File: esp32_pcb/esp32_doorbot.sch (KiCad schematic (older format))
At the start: 15 parts, among them J2 Conn_01x02_Female, J3 Conn_01x08, J4 Conn_01x06, Q1 2N7002E, U1 L7805, U2 74LVC2T45DC

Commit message: Use header that attaches to wesp32 board directly
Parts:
- J3: value Conn_01x08 -> ESP32; footprint Pin_Headers:Pin_Header_Straight_1x08 -> Pin_Headers:Pin_Header_Straight_2x10; symbol Connector_Generic:Conn_01x08 -> Connector_Generic:Conn_02x10_Odd_Even
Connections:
- no-connect marks 0 -> 12
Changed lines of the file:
@@
 Wire Wire Line
 	1650 3800 1500 3800
-Text GLabel 5200 1300 0    50   Input ~ 0
+Text GLabel 4050 1150 0    50   Input ~ 0
 12V
 $Comp
 L power:GND #PWR0104
 U 1 1 605FBF90
-P 5400 2050
-F 0 "#PWR0104" H 5400 1800 50  0001 C CNN
-F 1 "GND" H 5405 1877 50  0000 C CNN
-F 2 "" H 5400 2050 50  0001 C CNN
-F 3 "" H 5400 2050 50  0001 C CNN
-	1    5400 2050
-	1    0    0    -1
-$EndComp
-Text GLabel 5200 1500 0    50   Input ~ 0
+P 5550 1150
+F 0 "#PWR0104" H 5550 900 50  0001 C CNN
+F 1 "GND" H 5555 977 50  0000 C CNN
+F 2 "" H 5550 1150 50  0001 C CNN
+F 3 "" H 5550 1150 50  0001 C CNN
+	1    5550 1150
+	1    0    0    -1
+$EndComp
+Text GLabel 4050 1350 0    50   Input ~ 0
 DOOR
-Text GLabel 5200 1600 0    50   Input ~ 0
+Text GLabel 4050 1250 0    50   Input ~ 0
 WIEGAND_OUT1
-Text GLabel 5200 1700 0    50   Input ~ 0
+Text GLabel 4850 1350 2    50   Input ~ 0
 WIEGAND_OUT2
 $Comp
@@
 Text GLabel 5150 4950 1    50   Input ~ 0
 5V
-Text GLabel 5200 1400 0    50   Input ~ 0
+Text GLabel 4100 2050 0    50   Input ~ 0
 3.3V
-Wire Wire Line
-	5200 1300 5400 1300
-Wire Wire Line
-	5400 1400 5200 1400
-Wire Wire Line
-	5200 1500 5400 1500
-Wire Wire Line
-	5400 1600 5200 1600
-Wire Wire Line
-	5200 1700 5400 1700
 Text GLabel 5350 4950 1    50   Input ~ 0
 3.3V
@@
 Wire Wire Line
 	5250 6400 5250 6150
-Text GLabel 5200 1900 0    50   Input ~ 0
+Text GLabel 4050 1550 0    50   Input ~ 0
 READER_LED
-Text GLabel 5200 1800 0    50   Input ~ 0
+Text GLabel 4050 1450 0    50   Input ~ 0
 READER_BUZZ
 $Comp
-L Connector_Generic:Conn_01x08 J3
+L Connector_Generic:Conn_02x10_Odd_Even J3
 U 1 1 6063C556
-P 5600 1600
-F 0 "J3" H 5680 1592 50  0000 L CNN
-F 1 "Conn_01x08" H 5680 1501 50  0000 L CNN
-F 2 "Pin_Headers:Pin_Header_Straight_1x08" H 5600 1600 50  0001 C CNN
-F 3 "~" H 5600 1600 50  0001 C CNN
-	1    5600 1600
-	1    0    0    -1
-$EndComp
-Wire Wire Line
-	5200 1800 5400 1800
-Wire Wire Line
-	5400 1900 5200 1900
-Wire Wire Line
-	5400 2050 5400 2000
+P 4500 1650
+F 0 "J3" H 4500 2300 50  0000 L CNN
+F 1 "ESP32" H 4450 2200 50  0000 L CNN
+F 2 "Pin_Headers:Pin_Header_Straight_2x10" H 4500 1650 50  0001 C CNN
+F 3 "~" H 4500 1650 50  0001 C CNN
+	1    4500 1650
+	-1   0    0    1
+$EndComp
 $Comp
 L Connector_Generic:Conn_01x06 J4
@@
 Wire Wire Line
 	6400 1450 7350 1450
+Wire Wire Line
+	4200 1150 4050 1150
+Wire Wire Line
+	4050 1250 4200 1250
+Wire Wire Line
+	4200 1350 4050 1350
+Wire Wire Line
+	4050 1450 4200 1450
+Wire Wire Line
+	4200 1550 4050 1550
+Wire Wire Line
+	4100 2050 4200 2050
+Wire Wire Line
+	4700 1350 4850 1350
+Wire Wire Line
+	4700 1150 5550 1150
+NoConn ~ 4700 1250
+NoConn ~ 4700 1450
+NoConn ~ 4700 1550
+NoConn ~ 4700 1650
+NoConn ~ 4700 1750
+NoConn ~ 4700 1850
+NoConn ~ 4700 1950
+NoConn ~ 4700 2050
+NoConn ~ 4200 1950
+NoConn ~ 4200 1850
+NoConn ~ 4200 1750
+NoConn ~ 4200 1650
 $EndSCHEMATC

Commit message: Add part number for 2x10 pin header
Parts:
- J3: Digikey # (none) -> S6106-ND‎
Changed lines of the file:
@@
 F 2 "Pin_Headers:Pin_Header_Straight_2x10" H 4500 1650 50  0001 C CNN
 F 3 "~" H 4500 1650 50  0001 C CNN
+F 4 "S6106-ND‎" H 4500 1650 50  0001 C CNN "Digikey #"
 	1    4500 1650
 	-1   0    0    1

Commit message: Change schematic for regular ESP32, not a PoE version
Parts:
- removed J3: ESP32, Pin_Headers:Pin_Header_Straight_2x10, symbol Connector_Generic:Conn_02x10_Odd_Even
- removed J4: Conn_01x06, Pin_Headers:Pin_Header_Straight_1x06, symbol Connector_Generic:Conn_01x06
- added J1: Conn_01x07_Male, Pin_Headers:Pin_Header_Straight_1x07, symbol Connector:Conn_01x07_Male
- added J3: Barrel_Jack, Terminal_Blocks:TerminalBlock_Pheonix_MKDS1.5-2pol, symbol Connector:Barrel_Jack
- added J4: WROOM32_1, Pin_Headers:Pin_Header_Straight_1x15, symbol Connector:Conn_01x15_Female
- added J5: WROOM32_2, Pin_Headers:Pin_Header_Straight_1x15, symbol Connector:Conn_01x15_Female
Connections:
- net labels added: 24_32_SWITCH
- wire segments 51 -> 55
- no-connect marks 12 -> 21
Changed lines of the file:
@@
 Wire Wire Line
 	1650 3800 1500 3800
-Text GLabel 4050 1150 0    50   Input ~ 0
-12V
-$Comp
-L power:GND #PWR0104
-U 1 1 605FBF90
-P 5550 1150
-F 0 "#PWR0104" H 5550 900 50  0001 C CNN
-F 1 "GND" H 5555 977 50  0000 C CNN
-F 2 "" H 5550 1150 50  0001 C CNN
-F 3 "" H 5550 1150 50  0001 C CNN
-	1    5550 1150
-	1    0    0    -1
-$EndComp
-Text GLabel 4050 1350 0    50   Input ~ 0
+Text GLabel 9050 3300 2    50   Input ~ 0
 DOOR
-Text GLabel 4050 1250 0    50   Input ~ 0
+Text GLabel 7800 3300 0    50   Input ~ 0
 WIEGAND_OUT1
-Text GLabel 4850 1350 2    50   Input ~ 0
-WIEGAND_OUT2
 $Comp
 L Regulator_Linear:L7805 U1
@@
 Text GLabel 5150 4950 1    50   Input ~ 0
 5V
-Text GLabel 4100 2050 0    50   Input ~ 0
-3.3V
 Text GLabel 5350 4950 1    50   Input ~ 0
 3.3V
@@
 Wire Wire Line
 	5250 6400 5250 6150
-Text GLabel 4050 1550 0    50   Input ~ 0
+Text GLabel 9050 3100 2    50   Input ~ 0
 READER_LED
-Text GLabel 4050 1450 0    50   Input ~ 0
+Text GLabel 9050 3200 2    50   Input ~ 0
 READER_BUZZ
-$Comp
-L Connector_Generic:Conn_02x10_Odd_Even J3
-U 1 1 6063C556
-P 4500 1650
-F 0 "J3" H 4500 2300 50  0000 L CNN
-F 1 "ESP32" H 4450 2200 50  0000 L CNN
-F 2 "Pin_Headers:Pin_Header_Straight_2x10" H 4500 1650 50  0001 C CNN
-F 3 "~" H 4500 1650 50  0001 C CNN
-F 4 "S6106-ND‎" H 4500 1650 50  0001 C CNN "Digikey #"
-	1    4500 1650
-	-1   0    0    1
-$EndComp
-$Comp
-L Connector_Generic:Conn_01x06 J4
-U 1 1 60640874
-P 7550 1550
-F 0 "J4" H 7630 1542 50  0000 L CNN
-F 1 "Conn_01x06" H 7630 1451 50  0000 L CNN
-F 2 "Pin_Headers:Pin_Header_Straight_1x06" H 7550 1550 50  0001 C CNN
-F 3 "~" H 7550 1550 50  0001 C CNN
-	1    7550 1550
-	1    0    0    -1
-$EndComp
-Text GLabel 7150 1350 0    50   Input ~ 0
+Text GLabel 3550 1250 0    50   Input ~ 0
 12V
-Text GLabel 7150 1550 0    50   Input ~ 0
+Text GLabel 3550 1450 0    50   Input ~ 0
 WIEGAND_IN1
-Text GLabel 7150 1650 0    50   Input ~ 0
+Text GLabel 3550 1550 0    50   Input ~ 0
 WIEGAND_IN2
-Text GLabel 7150 1850 0    50   Input ~ 0
+Text GLabel 3550 1750 0    50   Input ~ 0
 READER_LED
-Text GLabel 7150 1750 0    50   Input ~ 0
+Text GLabel 3550 1650 0    50   Input ~ 0
 READER_BUZZ
 $Comp
 L power:GND #PWR0109
 U 1 1 60644B08
-P 6400 1450
-F 0 "#PWR0109" H 6400 1200 50  0001 C CNN
-F 1 "GND" H 6405 1277 50  0000 C CNN
-F 2 "" H 6400 1450 50  0001 C CNN
-F 3 "" H 6400 1450 50  0001 C CNN
-	1    6400 1450
-	1    0    0    -1
-$EndComp
-Wire Wire Line
-	7150 1350 7350 1350
-Wire Wire Line
-	7150 1550 7350 1550
-Wire Wire Line
-	7350 1650 7150 1650
-Wire Wire Line
-	7150 1750 7350 1750
+P 2800 1350
+F 0 "#PWR0109" H 2800 1100 50  0001 C CNN
+F 1 "GND" H 2805 1177 50  0000 C CNN
+F 2 "" H 2800 1350 50  0001 C CNN
+F 3 "" H 2800 1350 50  0001 C CNN
+	1    2800 1350
+	1    0    0    -1
+$EndComp
+Wire Wire Line
+	3550 1250 3750 1250
+Wire Wire Line
+	3550 1450 3750 1450
+Wire Wire Line
+	3750 1550 3550 1550
+Wire Wire Line
+	3550 1650 3750 1650
 Text GLabel 1200 950  1    50   Input ~ 0
 12V
@@
 	1200 1100 1200 950
 Wire Wire Line
-	7350 1850 7150 1850
-Wire Wire Line
-	6400 1450 7350 1450
-Wire Wire Line
-	4200 1150 4050 1150
-Wire Wire Line
-	4050 1250 4200 1250
-Wire Wire Line
-	4200 1350 4050 1350
-Wire Wire Line
-	4050 1450 4200 1450
-Wire Wire Line
-	4200 1550 4050 1550
-Wire Wire Line
-	4100 2050 4200 2050
-Wire Wire Line
-	4700 1350 4850 1350
-Wire Wire Line
-	4700 1150 5550 1150
-NoConn ~ 4700 1250
-NoConn ~ 4700 1450
-NoConn ~ 4700 1550
-NoConn ~ 4700 1650
-NoConn ~ 4700 1750
-NoConn ~ 4700 1850
-NoConn ~ 4700 1950
-NoConn ~ 4700 2050
-NoConn ~ 4200 1950
-NoConn ~ 4200 1850
-NoConn ~ 4200 1750
-NoConn ~ 4200 1650
+	2800 1350 3750 1350
+$Comp
+L Connector:Conn_01x07_Male J1
+U 1 1 608355C5
+P 3950 1550
+F 0 "J1" V 3785 1528 50  0000 C CNN
+F 1 "Conn_01x07_Male" V 3876 1528 50  0000 C CNN
+F 2 "Pin_Headers:Pin_Header_Straight_1x07" H 3950 1550 50  0001 C CNN
+F 3 "~" H 3950 1550 50  0001 C CNN
+	1    3950 1550
+	-1   0    0    1
+$EndComp
+Wire Wire Line
+	3550 1750 3750 1750
+Text GLabel 3550 1850 0    50   Input ~ 0
+24_32_SWITCH
+Wire Wire Line
+	3550 1850 3750 1850
+$Comp
+L Connector:Barrel_Jack J3
+U 1 1 60844277
+P 5750 1450
+F 0 "J3" H 5807 1775 50  0000 C CNN
+F 1 "Barrel_Jack" H 5807 1684 50  0000 C CNN
+F 2 "Terminal_Blocks:TerminalBlock_Pheonix_MKDS1.5-2pol" H 5800 1410 50  0001 C CNN
+F 3 "~" H 5800 1410 50  0001 C CNN
+	1    5750 1450
+	1    0    0    -1
+$EndComp
+$Comp
+L power:GND #PWR0102
+U 1 1 60845424
+P 6050 1700
+F 0 "#PWR0102" H 6050 1450 50  0001 C CNN
+F 1 "GND" H 6055 1527 50  0000 C CNN
+F 2 "" H 6050 1700 50  0001 C CNN
+F 3 "" H 6050 1700 50  0001 C CNN
+	1    6050 1700
+	1    0    0    -1
+$EndComp
+Text GLabel 6200 1350 2    50   Input ~ 0
+12V
+Wire Wire Line
+	6050 1350 6200 1350
+Wire Wire Line
+	6050 1550 6050 1700
+$Comp
+L power:GND #PWR0104
+U 1 1 6084B334
+P 7250 3400
+F 0 "#PWR0104" H 7250 3150 50  0001 C CNN
+F 1 "GND" H 7255 3227 50  0000 C CNN
+F 2 "" H 7250 3400 50  0001 C CNN
+F 3 "" H 7250 3400 50  0001 C CNN
+	1    7250 3400
+	1    0    0    -1
+$EndComp
+Text GLabel 7550 3500 0    50   Input ~ 0
+5V
+Text GLabel 7800 3200 0    50   Input ~ 0
+WIEGAND_OUT2
+$Comp
+L Connector:Conn_01x15_Female J4
+U 1 1 608610DB
+P 8150 2800
+F 0 "J4" H 8178 2826 50  0000 L CNN
+F 1 "WROOM32_1" H 8178 2735 50  0000 L CNN
+F 2 "Pin_Headers:Pin_Header_Straight_1x15" H 8150 2800 50  0001 C CNN
+F 3 "~" H 8150 2800 50  0001 C CNN
+	1    8150 2800
+	1    0    0    -1
+$EndComp
+$Comp
+L Connector:Conn_01x15_Female J5
+U 1 1 60861B21
+P 8700 2800
+F 0 "J5" H 8592 1875 50  0000 C CNN
+F 1 "WROOM32_2" H 8592 1966 50  0000 C CNN
+F 2 "Pin_Headers:Pin_Header_Straight_1x15" H 8700 2800 50  0001 C CNN
+F 3 "~" H 8700 2800 50  0001 C CNN
+	1    8700 2800
+	-1   0    0    1
+$EndComp
+Wire Wire Line
+	7550 3500 7950 3500
+Wire Wire Line
+	7950 3400 7250 3400
+Wire Wire Line
+	7800 3300 7950 3300
+Wire Wire Line
+	7950 3200 7800 3200
+Wire Wire Line
+	8900 3100 9050 3100
+Wire Wire Line
+	9050 3200 8900 3200
+Wire Wire Line
+	8900 3300 9050 3300
+Text GLabel 9050 3500 2    50   Input ~ 0
+3.3V
+Wire Wire Line
+	8900 3500 9050 3500
+Text GLabel 7800 3100 0    50   Input ~ 0
+24_32_SWITCH
+Wire Wire Line
+	7800 3100 7950 3100
+NoConn ~ 7950 3000
+NoConn ~ 7950 2900
+NoConn ~ 7950 2800
+NoConn ~ 7950 2700
+NoConn ~ 7950 2600
+NoConn ~ 7950 2500
+NoConn ~ 7950 2400
+NoConn ~ 7950 2300
+NoConn ~ 7950 2200
+NoConn ~ 7950 2100
+NoConn ~ 8900 2100
+NoConn ~ 8900 2200
+NoConn ~ 8900 2300
+NoConn ~ 8900 2400
+NoConn ~ 8900 2500
+NoConn ~ 8900 2600
+NoConn ~ 8900 2700
+NoConn ~ 8900 2800
+NoConn ~ 8900 2900
+NoConn ~ 8900 3000
+NoConn ~ 8900 3400
 $EndSCHEMATC

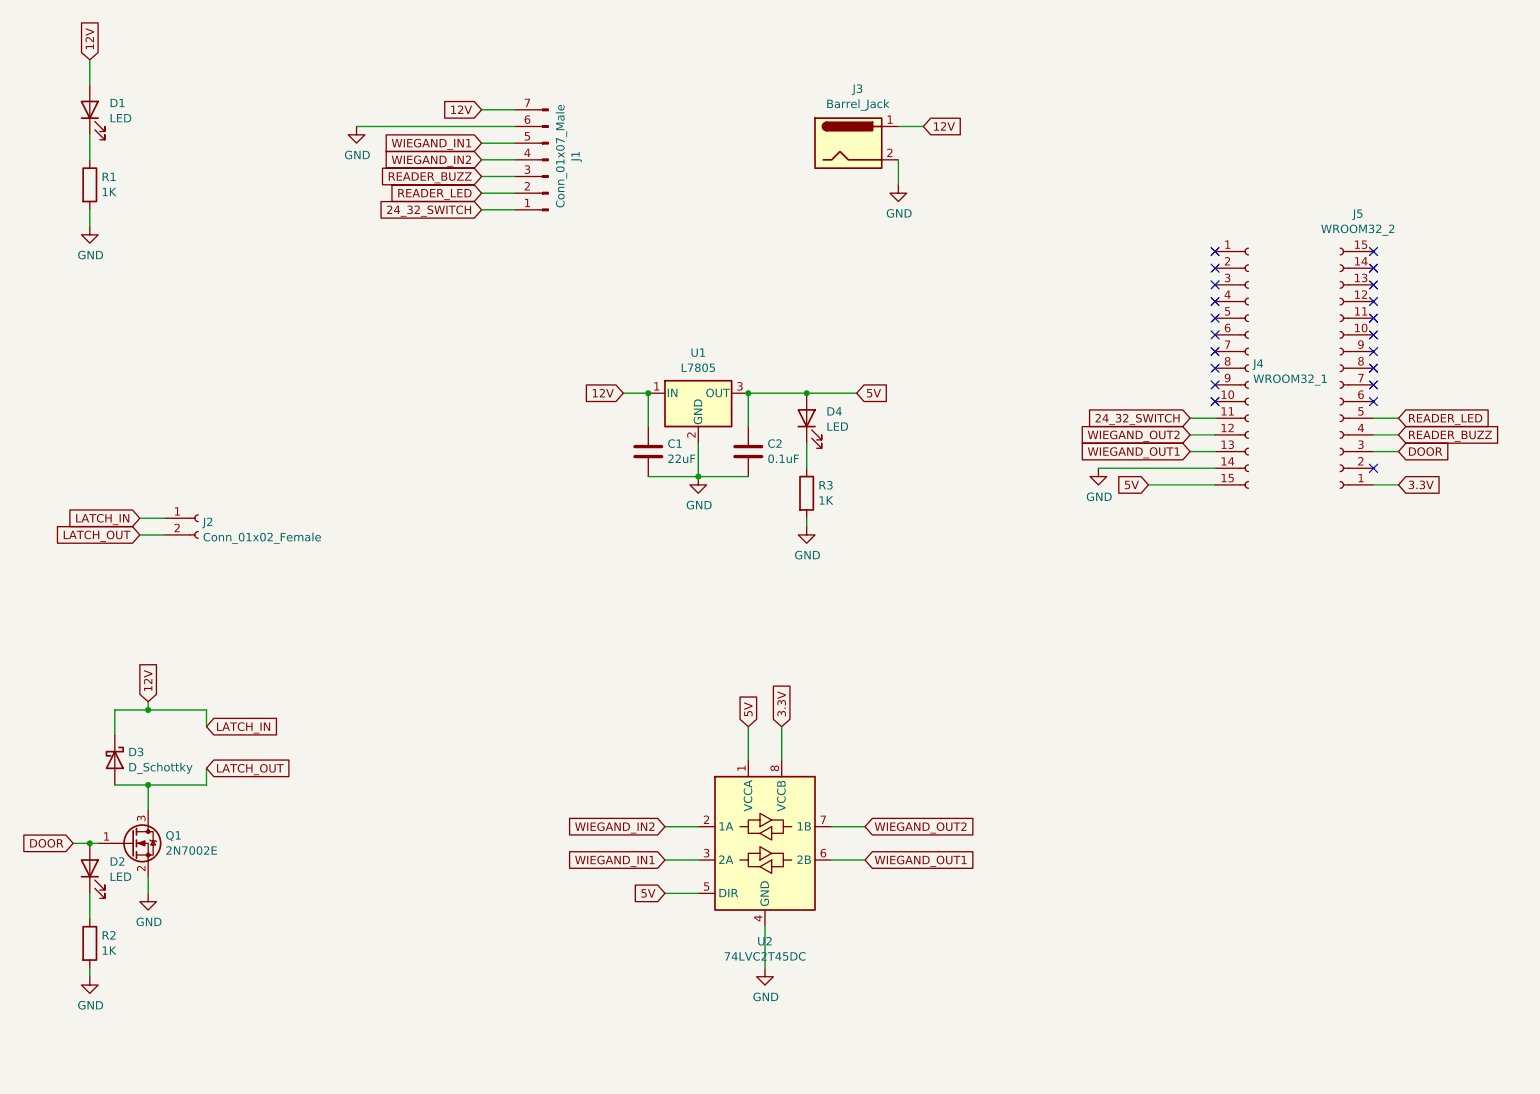
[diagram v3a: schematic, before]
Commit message: New layout for regular esp32
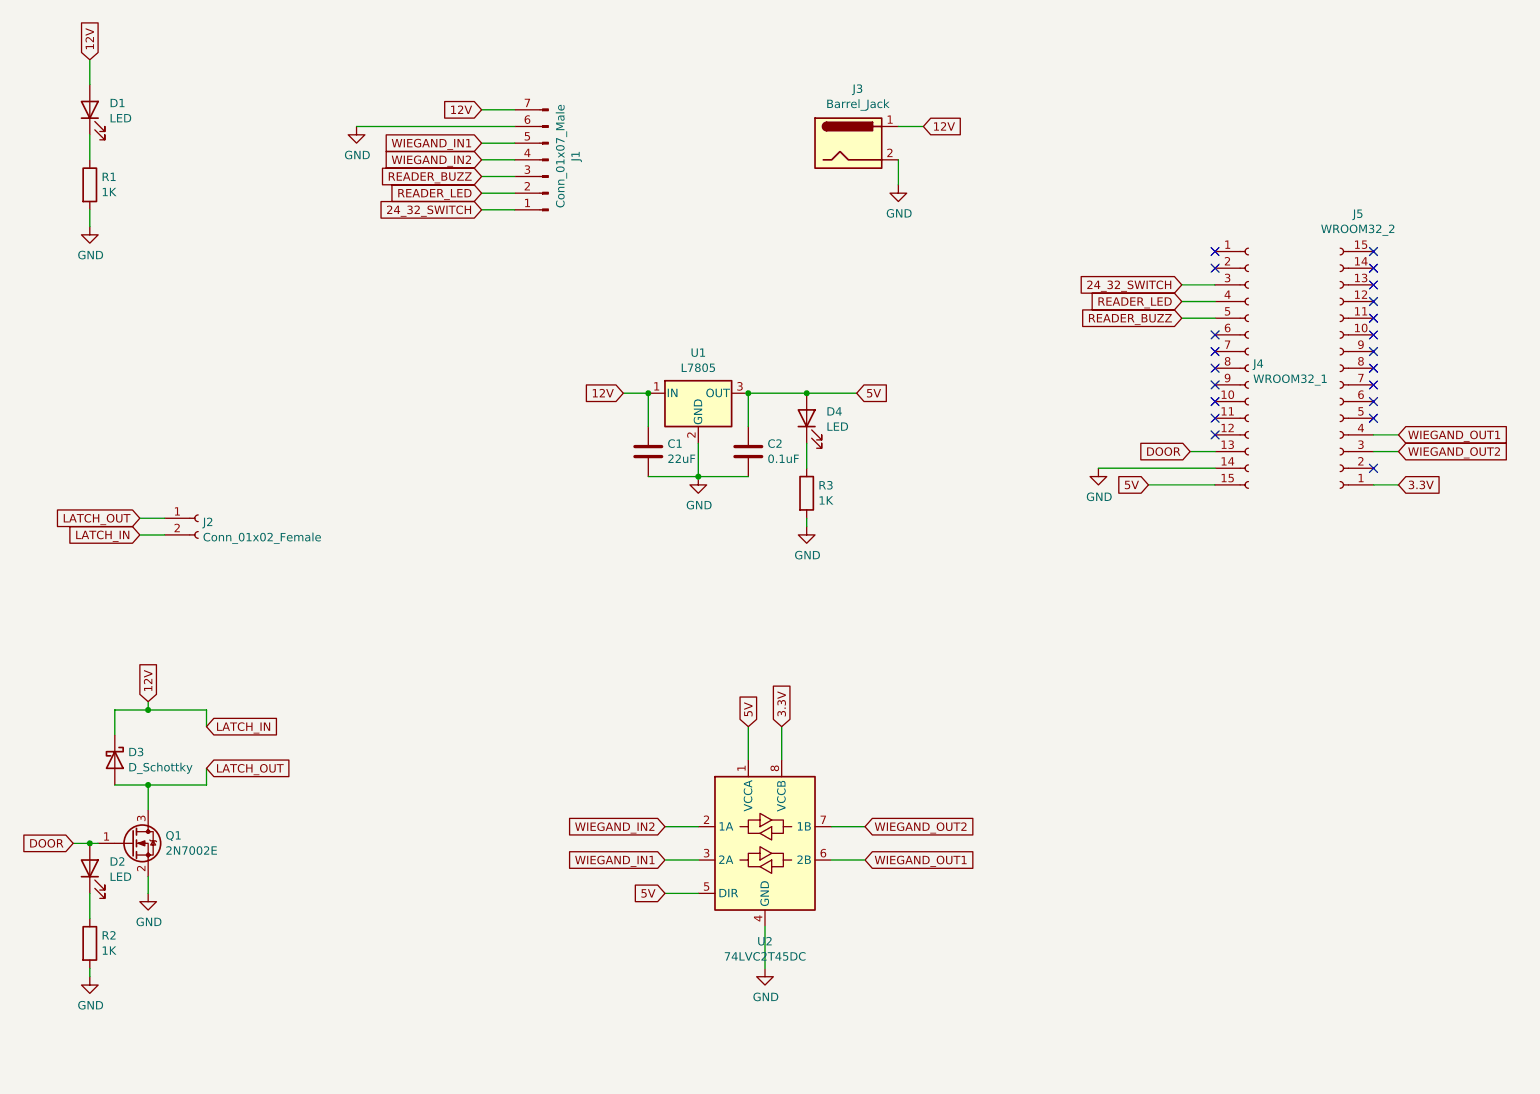
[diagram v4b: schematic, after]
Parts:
- D1, D2, D4: footprint LEDs:LED-0603 -> LEDs:LED_0603
- U2: footprint Tinkerforge-kicad:VSSOP8 -> tinkerforge-kicad:VSSOP8
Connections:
- net 12V: now also J2.2 (Pin_2); no longer J2.1 (Pin_1)
- net 24_32_SWITCH: now also J4.3 (Pin_3); no longer J4.11 (Pin_11)
- net DOOR: now also J4.13 (Pin_13); no longer J5.3 (Pin_3)
- net LATCH_OUT: now also J2.1 (Pin_1); no longer J2.2 (Pin_2)
- net READER_BUZZ: now also J4.5 (Pin_5); no longer J5.4 (Pin_4)
- net READER_LED: now also J4.4 (Pin_4); no longer J5.5 (Pin_5)
- net WIEGAND_OUT1: now also J5.4 (Pin_4); no longer J4.13 (Pin_13)
- net WIEGAND_OUT2: now also J5.3 (Pin_3); no longer J4.12 (Pin_12)
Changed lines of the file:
@@
 	1    0    0    -1
 $EndComp
+Text GLabel 1500 3800 0    50   Input ~ 0
+LATCH_IN
 Text GLabel 1500 3700 0    50   Input ~ 0
-LATCH_IN
-Text GLabel 1500 3800 0    50   Input ~ 0
 LATCH_OUT
 Wire Wire Line
@@
 Wire Wire Line
 	1650 3800 1500 3800
-Text GLabel 9050 3300 2    50   Input ~ 0
+Text GLabel 7800 3300 0    50   Input ~ 0
 DOOR
-Text GLabel 7800 3300 0    50   Input ~ 0
+Text GLabel 9050 3200 2    50   Input ~ 0
 WIEGAND_OUT1
 $Comp
@@
 F 0 "D4" V 5539 2982 50  0000 R CNN
 F 1 "LED" V 5448 2982 50  0000 R CNN
-F 2 "LEDs:LED-0603" H 5500 3100 50  0001 C CNN
+F 2 "LEDs:LED_0603" H 5500 3100 50  0001 C CNN
 F 3 "~" H 5500 3100 50  0001 C CNN
 F 4 "SML-D12U1WT86TR-ND" V 5500 3100 50  0001 C CNN "Digikey #"
@@
 F 0 "D2" V 1239 5682 50  0000 R CNN
 F 1 "LED" V 1148 5682 50  0000 R CNN
-F 2 "LEDs:LED-0603" H 1200 5800 50  0001 C CNN
+F 2 "LEDs:LED_0603" H 1200 5800 50  0001 C CNN
 F 3 "~" H 1200 5800 50  0001 C CNN
 F 4 "SML-D12U1WT86TR-ND" V 1200 5800 50  0001 C CNN "Digikey #"
@@
 F 0 "U2" H 5250 5061 50  0000 C CNN
 F 1 "74LVC2T45DC" H 5250 4970 50  0000 C CNN
-F 2 "Tinkerforge-kicad:VSSOP8" H 5250 4800 50  0001 C CNN
+F 2 "tinkerforge-kicad:VSSOP8" H 5250 4800 50  0001 C CNN
 F 3 "https://assets.nexperia.com/documents/data-sheet/74LVC_LVCH2T45.pdf" H 5500 5400 50  0001 C CNN
 F 4 "1727-4578-2-ND" H 5250 5650 50  0001 C CNN "Digikey #"
@@
 Wire Wire Line
 	5250 6400 5250 6150
-Text GLabel 9050 3100 2    50   Input ~ 0
+Text GLabel 7750 2400 0    50   Input ~ 0
 READER_LED
-Text GLabel 9050 3200 2    50   Input ~ 0
+Text GLabel 7750 2500 0    50   Input ~ 0
 READER_BUZZ
 Text GLabel 3550 1250 0    50   Input ~ 0
@@
 F 0 "D1" V 1239 1132 50  0000 R CNN
 F 1 "LED" V 1148 1132 50  0000 R CNN
-F 2 "LEDs:LED-0603" H 1200 1250 50  0001 C CNN
+F 2 "LEDs:LED_0603" H 1200 1250 50  0001 C CNN
 F 3 "~" H 1200 1250 50  0001 C CNN
 F 4 "SML-D12U1WT86TR-ND" V 1200 1250 50  0001 C CNN "Digikey #"
@@
 Text GLabel 7550 3500 0    50   Input ~ 0
 5V
-Text GLabel 7800 3200 0    50   Input ~ 0
+Text GLabel 9050 3300 2    50   Input ~ 0
 WIEGAND_OUT2
 $Comp
@@
 	7800 3300 7950 3300
 Wire Wire Line
-	7950 3200 7800 3200
-Wire Wire Line
-	8900 3100 9050 3100
-Wire Wire Line
 	9050 3200 8900 3200
 Wire Wire Line
@@
 Wire Wire Line
 	8900 3500 9050 3500
-Text GLabel 7800 3100 0    50   Input ~ 0
+Text GLabel 7750 2300 0    50   Input ~ 0
 24_32_SWITCH
-Wire Wire Line
-	7800 3100 7950 3100
 NoConn ~ 7950 3000
 NoConn ~ 7950 2900
@@
 NoConn ~ 7950 2700
 NoConn ~ 7950 2600
-NoConn ~ 7950 2500
-NoConn ~ 7950 2400
-NoConn ~ 7950 2300
 NoConn ~ 7950 2200
 NoConn ~ 7950 2100
@@
 NoConn ~ 8900 3000
 NoConn ~ 8900 3400
+NoConn ~ 7950 3100
+NoConn ~ 7950 3200
+NoConn ~ 8900 3100
+Wire Wire Line
+	7750 2300 7950 2300
+Wire Wire Line
+	7750 2400 7950 2400
+Wire Wire Line
+	7750 2500 7950 2500
 $EndSCHEMATC
